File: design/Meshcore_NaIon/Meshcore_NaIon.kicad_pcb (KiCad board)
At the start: 2 copper layers, 90 x 100 mm, 136 parts, among them J10 AVR ISP 3V3, J11 LC OUT - SYS 3V3, J12 LTO 2S + MID -, J3 I2C3V3, J4 GPS / T114 P3, J5 UART3V3, J7 SOLAR 12V, J8 Na-ion 1S, M1 NiceNano_CLONE_MODIFIED, M2 HT-RA62, Q1 AO3401A, Q2 AO3401A, Q3 2N7002K, SW1 USER, SW2 RESET, U1 CN3722, U2 TPS63802DLAR, U4 DS3231MZ+TRL, U6 ATtiny13A-SSU, U7 SN74LVC2G125, U8 LMV431A, U9 LMV431A

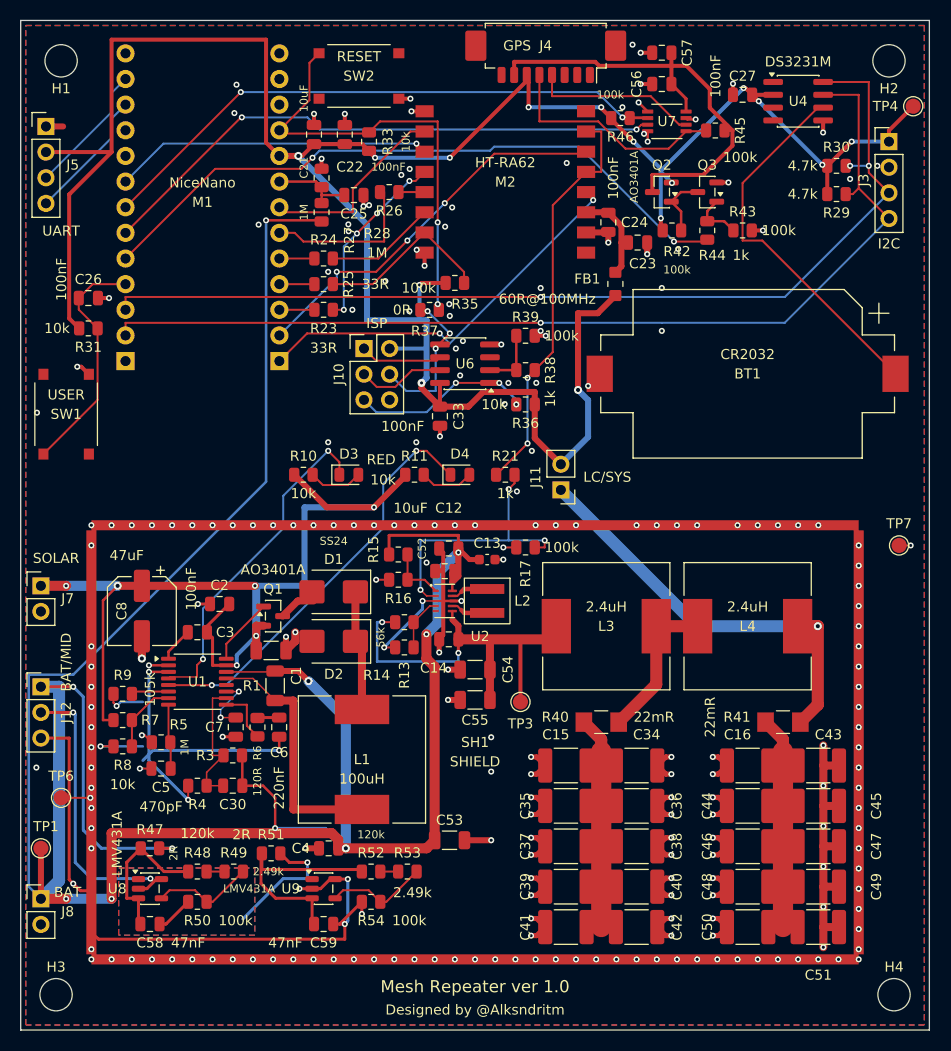
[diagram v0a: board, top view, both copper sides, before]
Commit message: Publish Mesh Repeater S4.16: routing fixes, COLD option and readable board labels
Update the editable KiCad project, seven-page schematic, portable footprints and 3D models, assembly variants, BOM, previews and independent CAD proofs. Preserve FakeTec GPIO compatibility. Manufacturing release remains paused.
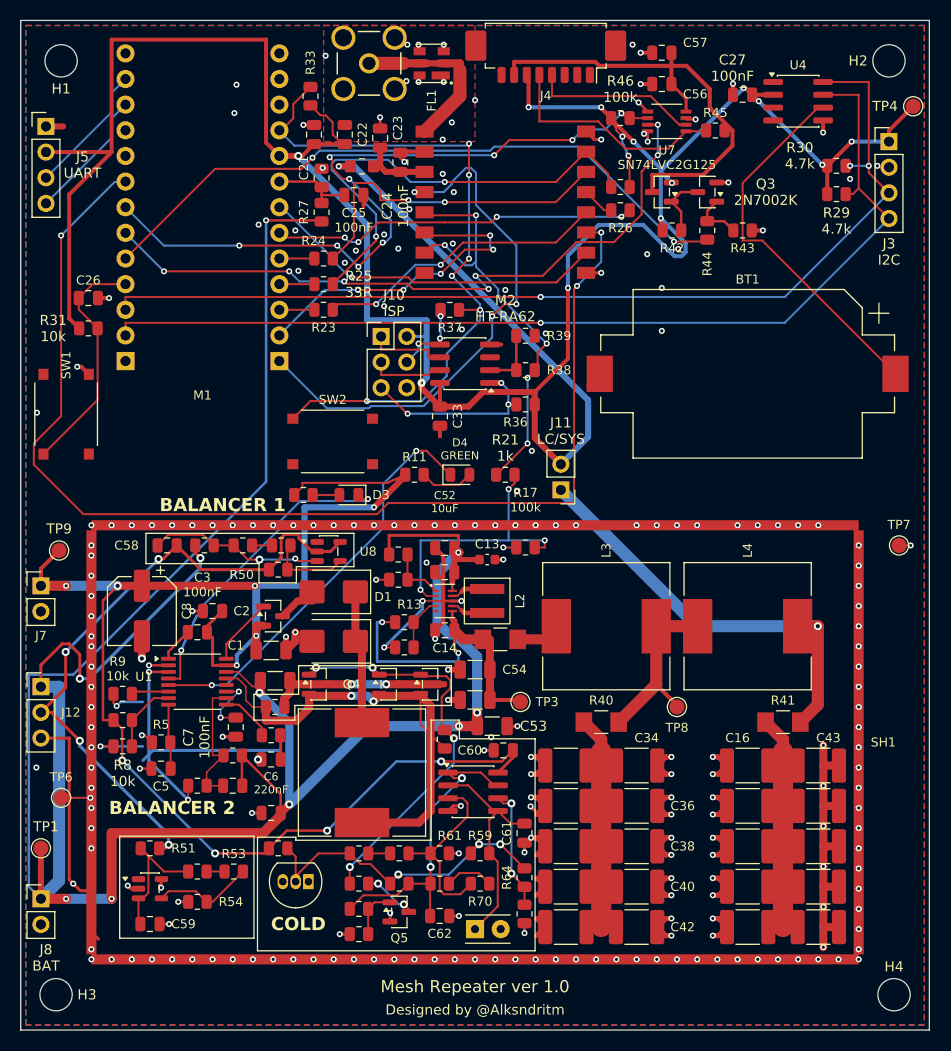
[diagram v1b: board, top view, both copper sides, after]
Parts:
- added C60: 100nF 100V X7R, Meshcore:C_0805_2012Metric, F.Cu at (47.8, 72.3)
- added C61: 1nF 100V C0G, Meshcore:C_0805_2012Metric, F.Cu at (49.9, 80.5)
- added C62: 100nF 100V X7R, Meshcore:C_0805_2012Metric, F.Cu at (41.5, 88.7)
- added FL1: S869M000S003, Meshcore:SAW_AEL_DCC6C_S869M000S003, F.Cu at (40.7, 4.25)
- added J13: SMA 50Ohm, Meshcore:SMA_KLS1_SMA002_B_Horizontal, F.Cu at (34.5, 4.25)
- added NT1: Cu link / cut for FL1, Meshcore:RF_Cut_Link_0p6, F.Cu at (40.7, 4.25)
- added Q4: AO3401A, Meshcore:SOT-23, F.Cu at (29.5, 65.8)
- added Q5: BSS138, Meshcore:SOT-23, F.Cu at (37.5, 88.3)
- added Q6: AO3401A, Meshcore:SOT-23, F.Cu at (36.5, 65.8)
- added Q7: AO3401A, Meshcore:SOT-23, F.Cu at (40.5, 65.8)
- added R55: 47mR 1%, Meshcore:R_Vishay_WSL1206_18, F.Cu at (47.5, 61.3)
- added R56: 1.8 ohm 1% 0.125W, Meshcore:R_0805_2012Metric, F.Cu at (25.2, 68.0)
- added R57: 47k 1% 0.125W, Meshcore:R_0805_2012Metric, F.Cu at (25.5, 82.0)
- added R58: 100k 1%, Meshcore:R_0805_2012Metric, F.Cu at (42.0, 71.2)
- added R59: 100k 1%, Meshcore:R_0805_2012Metric, F.Cu at (45.5, 82.5)
- added R60: 100k 1%, Meshcore:R_0805_2012Metric, F.Cu at (33.5, 82.5)
- added R61: 100k 1%, Meshcore:R_0805_2012Metric, F.Cu at (41.5, 82.5)
- added R62: 1M 1%, Meshcore:R_0805_2012Metric, F.Cu at (41.5, 85.5)
- added R63: 100k 1%, Meshcore:R_0805_2012Metric, F.Cu at (37.5, 85.5)
- added R64: 1.2M 1%, Meshcore:R_0805_2012Metric, F.Cu at (49.9, 84.9)
- added R65: 10k 1%, Meshcore:R_0805_2012Metric, F.Cu at (49.9, 88.5)
- added R66: 1k 1%, Meshcore:R_0805_2012Metric, F.Cu at (33.5, 88.0)
- added R67: 1M 1%, Meshcore:R_0805_2012Metric, F.Cu at (33.5, 90.5)
- added R68: 1k 1%, Meshcore:R_0805_2012Metric, F.Cu at (33.5, 85.5)
- added R69: 30k 1%, Meshcore:R_0805_2012Metric, F.Cu at (37.5, 82.5)
- added R70: 150k 1%, Meshcore:R_0805_2012Metric, F.Cu at (45.5, 85.5)
- added TH1: 10k NTC 1% B3988, Meshcore:NTC_TDK_B57861S_Onboard_or_Remote_P2.54mm, F.Cu at (45.0, 90.0)
- added TP8: FILTER_MID, Meshcore:TestPoint_Pad_D1.5mm, F.Cu at (65.0, 68.0)
- added TP9: SOLAR, Meshcore:TestPoint_Pad_D1.5mm, F.Cu at (3.80, 52.5)
- added U10: LM393XK, Meshcore:SOIC-8_3.9x4.9mm_P1.27mm, F.Cu at (44.8, 76.4)
- added U11: LM285Z-2.5G, Meshcore:TO-92_Inline, F.Cu at (28.5, 85.3)
- R27, R28: value 1M 0.1% -> 2.2M 0.1%
- R3: value 6.34k 0.1% -> 61.9k 0.1% <=25ppm/C
- R4: value 10k 0.1% -> 100k 0.1% <=25ppm/C
- moved U8 37.8 mm to (30.5, 52.6)
- moved C58 37.5 mm to (14.5, 52.0)
- moved SW2 36.3 mm to (30.9, 41.7)
- moved R50 33.9 mm to (25.5, 54.4)
- moved R49 32.6 mm to (25.8, 52.0)
- moved R48 32.6 mm to (22.0, 52.0)
- moved R47 30.5 mm to (18.2, 52.0), turned to 0 degrees
- moved FB1 27.7 mm to (33.8, 14.4), turned to 0 degrees
- moved C23 27.5 mm to (35.6, 11.7), turned to 90 degrees
- moved R26 23.0 mm to (59.4, 18.8), turned to 0 degrees
- moved C24 21.4 mm to (37.6, 14.1), turned to 90 degrees
- moved R35 19.0 mm to (59.4, 16.5), turned to 180 degrees
- moved R52 17.2 mm to (17.5, 84.3)
- moved R54 17.2 mm to (17.5, 87.3)
- moved C59 17.2 mm to (12.8, 89.5)
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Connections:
- L1 pad 2: /CS_P -> CS_P
- L3 pad 1: /2. Converter/SYS_PRE -> /2. Converter/SYS_LC_IN
- M2 pad 1: unconnected-(M2-ANT_/_IPEX_used-Pad1) -> /3. Modules/ANT_RF
- R1 pad 1: /CS_P -> CHG_CS_M
- U1 pad 13: /CS_P -> CS_P
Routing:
- net /3. Modules/RADIO_RXEN: track 31.5 -> 117.9 mm, vias 1 -> 3
- net SOLAR: track 91.0 -> 151.0 mm, vias 6 -> 10
- net CS_P: track 0.00 -> 50.8 mm, vias 0 -> 2
- net CHG_G_SHUNT: track 0.00 -> 40.2 mm, vias 0 -> 4
- net SYS_3V3: track 246.5 -> 285.0 mm
- net GND: track 269.8 -> 231.3 mm, vias 239 -> 240
- net /7. Thermal/CHG_VREF: track 0.00 -> 32.9 mm, vias 0 -> 3
- net /7. Thermal/CHG_WARM: track 0.00 -> 31.1 mm, vias 0 -> 2
- net Net-(M2-NSS): track 17.8 -> 47.6 mm, vias 0 -> 2
- net MCU_RESET: track 44.3 -> 70.8 mm, vias 2 -> 6
- net /CS_P: track 25.1 -> 0.00 mm
- net Net-(M2-MOSI): track 11.0 -> 34.0 mm, vias 0 -> 2
- net /7. Thermal/CHG_TSENSE: track 0.00 -> 22.5 mm
- net Net-(M1-P0.02_/_MISO): track 15.6 -> 36.4 mm, vias 0 -> 4
- net BAT: track 282.7 -> 262.4 mm
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- removed copper zone on B.Cu, net LTO_MID
- removed copper zone on F.Cu, net LTO_MID
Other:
- board text added: "1 NTC"
- board text added: "1 RF"
- board text added: "BAL1 x1.5"
- board text added: "BAL2 x1.25"
- board text added: "BALANCER 1"
- board text added: "BALANCER 2"
- board text added: "BT1"
- board text added: "BT1 CR2032"
- board text added: "C1"
- board text added: "C1 10uF"
- board text added: "C12 10uF"
- board text added: "C13"
- board text added: "C13 100nF"
- board text added: "C14"
- board text added: "C14 22uF"
- board text added: "C15 100uF"
- board text added: "C16"
- board text added: "C16 100uF"
- board text added: "C2"
- board text added: "C2 100nF"
- board text added: "C21"
- board text added: "C21 10uF"
- board text added: "C22"
- board text added: "C22 100nF"
- board text added: "C23"
- board text added: "C23 22uF"
- board text added: "C24 100nF"
- board text added: "C25 100nF"
- board text added: "C26"
- board text added: "C26 100nF"
- board text added: "C27 100nF"
- board text added: "C3 100nF"
- board text added: "C30 Na:12pF LTO:6.8pF"
- board text added: "C33"
- board text added: "C33 100nF"
- board text added: "C34"
- board text added: "C34 100uF"
- board text added: "C35 100uF"
- board text added: "C36"
- board text added: "C36 100uF"
- board text added: "C37 100uF"
- board text added: "C38"
- board text added: "C38 100uF"
- board text added: "C39 100uF"
- board text added: "C40"
- board text added: "C40 100uF"
- board text added: "C41 100uF"
- board text added: "C42"
- board text added: "C42 100uF"
- board text added: "C43"
- board text added: "C43 100uF"
- board text added: "C44 100uF"
- board text added: "C45 100uF"
- board text added: "C46 100uF"
- board text added: "C47 100uF"
- board text added: "C48 100uF"
- board text added: "C49 100uF"
- board text added: "C5"
- board text added: "C5 470pF"
- board text added: "C50 100uF"
- board text added: "C51 100uF"
- board text added: "C52 10uF"
- board text added: "C53"
- board text added: "C54"
- board text added: "C55"
- board text added: "C56"
- board text added: "C56 100nF"
- board text added: "C57"
- board text added: "C57 10uF"
- board text added: "C58"
- board text added: "C58 47nF"
- board text added: "C59"
- board text added: "C59 47nF"
- board text added: "C6 220nF"
- board text added: "C60"
- board text added: "C60 100nF"
- board text added: "C61"
- board text added: "C61 1nF"
- board text added: "C62"
- board text added: "C62 100nF"
- board text added: "C7 100nF"
- board text added: "C8"
- board text added: "C8 47uF"
- board text added: "CHG x1.25"
- board text added: "CHG x1.5"
- board text added: "CHG x1.75"
- board text added: "COLD"
- board text added: "COLD x1.25"
- board text added: "COLD x1.5"
- board text added: "COLD x1.75"
- board text added: "D1"
- board text added: "D1 SS24"
- board text added: "D2 SS24"
- board text added: "D3"
- board text added: "D3 RED"
- board text added: "D4 GREEN"
- board text added: "FB1 60R@100MHz"
- board text added: "FL1"
- board text added: "FL1 S869M000S003"
- board text added: "H1"
- board text added: "H2"
- board text added: "H3"
- board text added: "H4"
- board text added: "J12"
- board text added: "J12 BAT/ MID"
- board text added: "J13 SMA"
- board text added: "J4"
- board text added: "J7"
- board text added: "L1 100uH"
- board text added: "L2"
- board text added: "L2 0.47uH"
- board text added: "L3"
- board text added: "L3 2.4uH"
- board text added: "L4"
- board text added: "L4 2.4uH"
- board text added: "LC x1.25"
- board text added: "M1"
- board text added: "M1 NiceNano"
- board text added: "M2 HT-RA62"
- board text added: "NT1"
- board text added: "PARTS x1.25"
- board text added: "PARTS x1.5"
- board text added: "Q1 AO3401A"
- board text added: "Q2 AO3401A"
- board text added: "Q3 2N7002K"
- board text added: "Q4"
- board text added: "Q4 AO3401A"
- board text added: "Q5"
- board text added: "Q5 BSS138"
- board text added: "Q6 AO3401A"
- board text added: "Q7 AO3401A"
- board text added: "R1 0.28R"
- board text added: "R10 10k"
- board text added: "R11"
- board text added: "R11 10k"
- board text added: "R13"
- board text added: "R13 56k"
- board text added: "R14 10k"
- board text added: "R15 Na:40.2k LTO:130k"
- board text added: "R16 Na:49.9k LTO:49.9k"
- board text added: "R17 100k"
- board text added: "R21 1k"
- board text added: "R23"
- board text added: "R23 33R"
- board text added: "R24"
- board text added: "R24 33R"
- board text added: "R25 33R"
- board text added: "R26"
- board text added: "R26 33R"
- board text added: "R27"
- board text added: "R27 2.2M"
- board text added: "R28 2.2M"
- board text added: "R29 4.7k"
- board text added: "R3 Na:61.9k LTO:121k"
- board text added: "R30 4.7k"
- board text added: "R31 10k"
- board text added: "R33"
- board text added: "R33 10k"
- board text added: "R35 100k"
- board text added: "R36"
- board text added: "R36 10k"
- board text added: "R37"
- board text added: "R37 0R"
- board text added: "R38"
- board text added: "R38 1k"
- board text added: "R39"
- board text added: "R39 100k"
- board text added: "R4 Na:100k LTO:100k"
- board text added: "R40"
- board text added: "R40 22mR"
- board text added: "R41"
- board text added: "R41 22mR"
- board text added: "R42"
- board text added: "R42 100k"
- board text added: "R43"
- board text added: "R43 100k"
- board text added: "R44"
- board text added: "R44 1k"
- board text added: "R45"
- board text added: "R45 100k"
- board text added: "R46 100k"
- board text added: "R47 2R"
- board text added: "R48 120k"
- board text added: "R49 2.49k"
- board text added: "R5"
- board text added: "R5 1M"
- board text added: "R50"
- board text added: "R50 100k"
- board text added: "R51"
- board text added: "R51 2R"
- board text added: "R52 120k"
- board text added: "R53"
- board text added: "R53 2.49k"
- board text added: "R54"
- board text added: "R54 100k"
- board text added: "R55 47mR"
- board text added: "R56 Na:1.8R LTO:0R"
- board text added: "R57 47k"
- board text added: "R58 100k"
- board text added: "R59"
- board text added: "R59 100k"
- board text added: "R6 120R"
- board text added: "R60 100k"
- board text added: "R61"
- board text added: "R61 100k"
- board text added: "R62 1M"
- board text added: "R63 100k"
- board text added: "R64"
- board text added: "R64 1.2M"
- board text added: "R65 10k"
- board text added: "R66 1k"
- board text added: "R67 1M"
- board text added: "R68 1k"
- board text added: "R69 30k"
- board text added: "R7 105k"
- board text added: "R70"
- board text added: "R70 150k"
- board text added: "R8 10k"
- board text added: "R9 10k"
- board text added: "RF x1.25"
- board text added: "SH1"
- board text added: "SH1 SHIELD"
- board text added: "SW1"
- board text added: "SW1 USER"
- board text added: "SW2"
- board text added: "SW2 RESET"
- board text added: "TH1 10k NTC"
- board text added: "TH1 NTC"
- board text added: "TP1"
- board text added: "TP3"
- board text added: "TP4"
- board text added: "TP6"
- board text added: "TP7"
- board text added: "TP8"
- board text added: "TP9"
- board text added: "TPS x1.25"
- board text added: "TPS x1.5"
- board text added: "U1"
- board text added: "U1 CN3722"
- board text added: "U10 LM393XK"
- board text added: "U11 LM285Z-2.5G"
- board text added: "U2 TPS63802DLAR"
- board text added: "U4"
- board text added: "U4 DS3231M"
- board text added: "U7 SN74LVC2G125"
- board text added: "U8"
- board text added: "U8 LMV431A"
- board text added: "U9 LMV431A"
- board text added: "WDT x1.25"
- board text removed: "C1 10uF C3 100nF C7 100nF R1 0.28R R9 10k U1 CN3722"
- board text removed: "C13 100nF C14 22uF C52 10uF D2 SS24 D4 GREEN L2 0.47uH R14 10k U2 TPS63802DLAR"
- board text removed: "C15 100uF C34 100uF C35 100uF C36 100uF C37 100uF C38 100uF C39 100uF C40 100uF C41 100uF C42 100uF"
- board text removed: "C16 100uF C43 100uF C44 100uF C45 100uF C46 100uF C47 100uF C48 100uF C49 100uF C50 100uF C51 100uF"
- board text removed: "C23 22uF C56 100nF C57 10uF Q3 2N7002K U7 SN74LVC2G125"
- board text removed: "C25 100nF R24 33R R26 33R"
- board text removed: "C30 Na:12pF LTO:6.8pF R3 Na:6.34k LTO:13k R4 Na:10k LTO:10.5k"
- board text removed: "R15 Na:40.2k LTO:130k R16 Na:49.9k LTO:49.9k"

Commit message: Publish S4.21 PCB and validated Rezonit manufacturing package
Update the public project to the accepted single-board S4.21 design, keeping
the user's manual routing improvements and removing SH1 and TP6.

Include the full editable KiCad project and local assets, three assembly BOM
variants, current assembly notes, eight-page schematic PDF, board views and
a clean nine-file Gerber/Excellon ZIP for Rezonit.

Validation: layout 29/29, power 14/14, CAM 59/59, publication integrity 18/18.
The committed native board and manufacturing ZIP match the verified byte
hashes. Preserve the existing licensing notices and watchdog source.
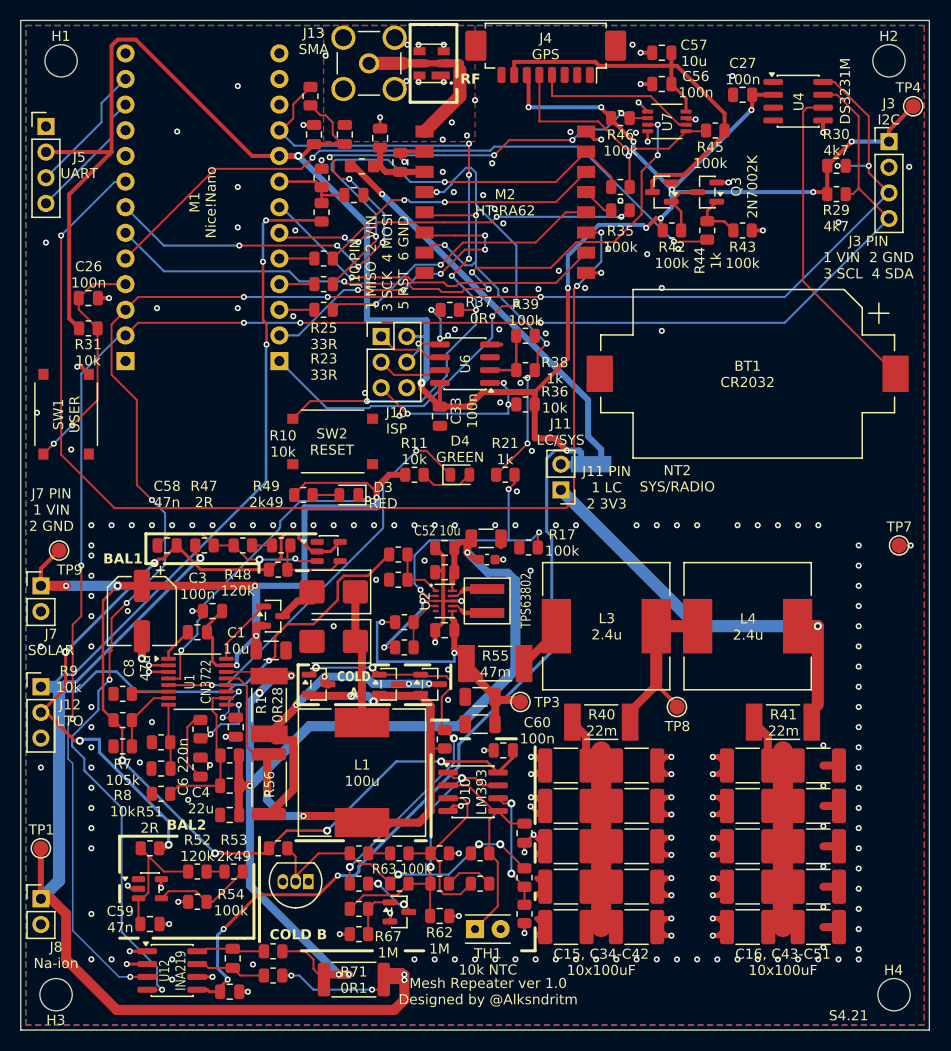
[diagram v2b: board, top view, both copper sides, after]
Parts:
- removed SH1: CUSTOM_SHIELD_FRAME, Meshcore:Shield_Frame_76x43
- removed TP6: GND, Meshcore:TestPoint_Pad_D1.5mm
- added C63: 100nF 50V X7R, Meshcore:C_0805_2012Metric, F.Cu at (20.7, 96.2)
- added C64: 100nF 50V X7R, Meshcore:C_0805_2012Metric, F.Cu at (21.0, 92.9)
- added NT2: 3V3 STAR, Meshcore:NetTie_2_SMD_Power_Star_A3, B.Cu at (56.5, 44.0)
- added R71: 0.1R 1% 1W, Meshcore:R_2512_6332Metric__A3_R71, F.Cu at (33.0, 95.0)
- added R72: 10R 1%, Meshcore:R_0805_2012Metric, F.Cu at (25.0, 92.2)
- added R73: 10R 1%, Meshcore:R_0805_2012Metric, F.Cu at (25.0, 94.6)
- added U12: INA219AIDR, Meshcore:SOIC-8_3.9x4.9mm_P1.27mm, F.Cu at (15.0, 94.1)
- R1: footprint Meshcore:R_1206_3216Metric -> Meshcore:R_Vishay_WSL2512_A3__A3_R1
- R40: footprint Meshcore:R_Vishay_WSL1206_18 -> Meshcore:R_Vishay_WSL2512_A3__A3_R40
- R41: footprint Meshcore:R_Vishay_WSL1206_18 -> Meshcore:R_Vishay_WSL2512_A3__A3_R41
- R55: footprint Meshcore:R_Vishay_WSL1206_18 -> Meshcore:R_Vishay_WSL2512_A3__A3_R55
- R56: value 1.8 ohm 1% 0.125W -> 1.8R 1% 1W; footprint Meshcore:R_0805_2012Metric -> Meshcore:R_2512_6332Metric__A3_R56
- moved C53 18.6 mm to (46.1, 51.3)
- moved R56 7.67 mm to (24.6, 75.7), turned to -90 degrees
- moved C6 7.04 mm to (17.8, 74.0), turned to 90 degrees
- moved R6 7.03 mm to (17.8, 70.2), turned to 90 degrees
- moved C4 4.10 mm to (20.7, 78.7)
- moved R4 3.69 mm to (13.9, 76.6)
- moved C54 2.75 mm to (45.5, 67.0)
- moved R1 2.47 mm to (24.6, 67.8), turned to 90 degrees
- moved C55 2.45 mm to (45.5, 69.7)
- moved R55 2.45 mm to (47.0, 63.7)
- moved C30 0.30 mm to (20.7, 75.8)
- moved R3 0.30 mm to (20.7, 72.8)
- moved R17 0.30 mm to (50.3, 52.2)
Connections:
- net /3. Modules/RADIO_3V3 renamed /3. Modules/RADIO_LOCAL_3V3
- C12 pad 1: BAT -> BAT_SYS
- C13 pad 1: BAT -> BAT_SYS
- C30 pad 1: BAT -> BAT_SYS
- C4 pad 1: BAT -> BAT_SYS
- C52 pad 1: BAT -> BAT_SYS
- C53 pad 1: BAT -> BAT_SYS
- FB1 pad 1: SYS_3V3 -> RADIO_3V3
- R1 pad 2: BAT -> BAT_SYS
- R3 pad 1: BAT -> BAT_SYS
- U1 pad 14: BAT -> BAT_SYS
- U2 pad 10: BAT -> BAT_SYS
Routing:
- net BAT_SYS: track 0.00 -> 114.4 mm, vias 0 -> 6
- net GND: track 231.3 -> 135.4 mm, vias 240 -> 237
- net SCL: track 99.8 -> 177.7 mm, vias 3 -> 9
- net SDA: track 99.7 -> 168.8 mm, vias 1 -> 6
- net BAT: track 262.4 -> 214.2 mm, vias 10 -> 9
- net RADIO_3V3: track 0.00 -> 40.0 mm, vias 0 -> 1
- net SYS_3V3: track 285.0 -> 312.4 mm, vias 15 -> 17
- net CHG_CS_M: track 17.8 -> 32.7 mm, vias 2 -> 4
- net Net-(U12-IN-): track 0.00 -> 7.08 mm
- net Net-(U12-IN+): track 0.00 -> 6.82 mm
- net CS_P: track 50.8 -> 56.9 mm, vias 2 -> 4
- net /4. RTC_IO/RTC_BAT: track 37.4 -> 31.9 mm
- net Net-(M2-MOSI): track 34.0 -> 28.9 mm
- net /3. Modules/RADIO_RXEN: track 117.9 -> 112.8 mm
- net Net-(C6-Pad1): track 2.42 -> 7.35 mm
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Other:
- board text added: "BAL1"
- board text added: "BAL2"
- board text added: "C1 10u"
- board text added: "C12 10u"
- board text added: "C13 100n"
- board text added: "C14 22u"
- board text added: "C15, C34-C42 10x100uF"
- board text added: "C16, C43-C51 10x100uF"
- board text added: "C2 100n"
- board text added: "C21 10u"
- board text added: "C22 100n"
- board text added: "C23 22u"
- board text added: "C24 100n"
- board text added: "C25 100n"
- board text added: "C26 100n"
- board text added: "C27 100n"
- board text added: "C3 100n"
- board text added: "C30 N12p L6.8p"
- board text added: "C33 100n"
- board text added: "C4 22u"
- board text added: "C5 470p"
- board text added: "C52 10u"
- board text added: "C53 DNP"
- board text added: "C54 DNP"
- board text added: "C55 DNP"
- board text added: "C56 100n"
- board text added: "C57 10u"
- board text added: "C58 47n"
- board text added: "C59 47n"
- board text added: "C6 220n"
- board text added: "C60 100n"
- board text added: "C61 1n"
- board text added: "C62 100n"
- board text added: "C63 100n"
- board text added: "C64 100n"
- board text added: "C7 100n"
- board text added: "C8 47u"
- board text added: "COLD A"
- board text added: "COLD B"
- board text added: "DS3231M"
- board text added: "FB1 60R"
- board text added: "FL1 S869M000 S003 NT1 CUT"
- board text added: "J10 PIN 1 MISO 2 VIN 3 SCK 4 MOSI 5 RST 6 GND"
- board text added: "J11 PIN 1 LC 2 3V3"
- board text added: "J12 PIN 1 BAT+ 2 MID 3 GND"
- board text added: "J13 PIN 1 RF 2 GND"
- board text added: "J3 PIN 1 VIN 2 GND 3 SCL 4 SDA"
- board text added: "J4 PIN 1 NC 2 NC 3 NC 4 RX 5 TX 6 BACKUP 7 POWER 8 GND"
- board text added: "J5 PIN UART 1 GND 2 VIN 3 TX 4 RX"
- board text added: "J7 PIN 1 VIN 2 GND"
- board text added: "J8 Na-ion"
- board text added: "J8 PIN 1 BAT+ 2 GND"
- board text added: "L1 100u"
- board text added: "L2 0.47u"
- board text added: "L3 2.4u"
- board text added: "L4 2.4u"
- board text added: "M1 Nice!Nano"
- board text added: "Mesh Repeater ver 1.0 Designed by @Alksndritm"
- board text added: "N: Na-ion / L: LTO 2S"
- board text added: "NT2 SYS/RADIO"
- board text added: "R1 0R28"
- board text added: "R15 N40k2 L130k"
- board text added: "R16 49k9"
- board text added: "R27 2M2"
- board text added: "R28 2M2"
- board text added: "R29 4k7"
- board text added: "R3 N61k9 L121k"
- board text added: "R30 4k7"
- board text added: "R4 100k"
- board text added: "R40 22m"
- board text added: "R41 22m"
- board text added: "R49 2k49"
- board text added: "R53 2k49"
- board text added: "R55 47m"
- board text added: "R56"
- board text added: "R56 N1R8 L0R"
- board text added: "R56: 0R без ХОЛОДА"
- board text added: "R64 1M2"
- board text added: "R71 0R1"
- board text added: "R72 10R"
- board text added: "R73 10R"
- board text added: "RF"
- board text added: "S4.21"
- board text added: "TPS63802"
- board text added: "U10 LM393"
- board text added: "U11 LM285-2.5"
- board text added: "U12 INA219"
- board text added: "U2"
- board text added: "U6"
- board text added: "U7"
- board text added: "U7 74LVC2G125"
- board text added: "U8 LMV 431A"
- board text added: "USB: снять J11"
- board text removed: "1"
- board text removed: "1 BAT+"
- board text removed: "1 GND"
- board text removed: "1 LC_OUT"
- board text removed: "1 MISO"
- board text removed: "1 NC/RST"
- board text removed: "1 NTC"
- board text removed: "1 RF"
- board text removed: "1 SOLAR+"
- board text removed: "1 VIN"
- board text removed: "2"
- board text removed: "2 GND"
- board text removed: "2 MID"
- board text removed: "2 NC/PPS"
- board text removed: "2 SYS_3V3"
- board text removed: "2 VIN"
- board text removed: "3"
- board text removed: "3 GND"
- board text removed: "3 NC/WAKE"
- board text removed: "3 SCK"
- board text removed: "3 SCL"
- board text removed: "3 TX"
- board text removed: "4"
- board text removed: "4 MOSI"
- board text removed: "4 RX"
- board text removed: "4 SDA"
- board text removed: "5"
- board text removed: "5 RESET"
- board text removed: "5 TX"
- board text removed: "6"
- board text removed: "6 BACKUP"
- board text removed: "6 GND"
- board text removed: "7"
- board text removed: "7 POWER"
- board text removed: "8"
- board text removed: "8 GND"
- board text removed: "BAL1 x1.5"
- board text removed: "BAL2 x1.25"
- board text removed: "BALANCER 1"
- board text removed: "BALANCER 2"
- board text removed: "BT1"
- board text removed: "BT1 +"
- board text removed: "BT1 -"
- board text removed: "C1"
- board text removed: "C1 10uF"
- board text removed: "C12 10uF"
- board text removed: "C13"
- board text removed: "C13 100nF"
- board text removed: "C14"
- board text removed: "C14 22uF"
- board text removed: "C15 100uF"
- board text removed: "C16"
- board text removed: "C16 100uF"
- board text removed: "C2"
- board text removed: "C2 100nF"
- board text removed: "C21"
- board text removed: "C21 10uF"
- board text removed: "C22"
- board text removed: "C22 100nF"
- board text removed: "C23"
- board text removed: "C23 22uF"
- board text removed: "C24 100nF"
- board text removed: "C25 100nF"
- board text removed: "C26"
- board text removed: "C26 100nF"
- board text removed: "C27 100nF"
- board text removed: "C3 100nF"
- board text removed: "C30 Na:12pF LTO:6.8pF"
- board text removed: "C33"
- board text removed: "C33 100nF"
- board text removed: "C34"
- board text removed: "C34 100uF"
- board text removed: "C35 100uF"
- board text removed: "C36"
- board text removed: "C36 100uF"
- board text removed: "C37 100uF"
- board text removed: "C38"
- board text removed: "C38 100uF"
- board text removed: "C39 100uF"
- board text removed: "C4 22uF"
- board text removed: "C40"
- board text removed: "C40 100uF"
- board text removed: "C41 100uF"
- board text removed: "C42"
- board text removed: "C42 100uF"
- board text removed: "C43"
- board text removed: "C43 100uF"
- board text removed: "C44 100uF"
- board text removed: "C45 100uF"
- board text removed: "C46 100uF"
- board text removed: "C47 100uF"
- board text removed: "C48 100uF"
- board text removed: "C49 100uF"
- board text removed: "C5"
- board text removed: "C5 470pF"
- board text removed: "C50 100uF"
- board text removed: "C51 100uF"
- board text removed: "C52 10uF"
- board text removed: "C53"
- board text removed: "C54"
- board text removed: "C55"
- board text removed: "C56"
- board text removed: "C56 100nF"
- board text removed: "C57"
- board text removed: "C57 10uF"
- board text removed: "C58"
- board text removed: "C58 47nF"
- board text removed: "C59"
- board text removed: "C59 47nF"
- board text removed: "C6 220nF"
- board text removed: "C60"
- board text removed: "C60 100nF"
- board text removed: "C61"
- board text removed: "C61 1nF"
- board text removed: "C62"
- board text removed: "C62 100nF"
- board text removed: "C7 100nF"
- board text removed: "C8"
- board text removed: "C8 47uF"
- board text removed: "CHG x1.25"
- board text removed: "CHG x1.5"
- board text removed: "CHG x1.75"
- board text removed: "COLD"
- board text removed: "COLD x1.25"
- board text removed: "COLD x1.5"
- board text removed: "COLD x1.75"
- board text removed: "CUSTOM LID 76x43 H14"
- board text removed: "D1"
- board text removed: "D3"
- board text removed: "Designed by @Alksndritm"
- board text removed: "FB1 60R@100MHz"
- board text removed: "FL1"
- board text removed: "FL1 S869M000S003"
- board text removed: "J12"
- board text removed: "J12 BAT/ MID"
- board text removed: "J4"
- board text removed: "J7"
- board text removed: "J8 BAT"
- board text removed: "L1 100uH"
- board text removed: "L2"
- board text removed: "L2 0.47uH"
- board text removed: "L3"
- board text removed: "L3 2.4uH"
- board text removed: "L4"
- board text removed: "L4 2.4uH"
- board text removed: "LC x1.25"
- board text removed: "M1"
- board text removed: "M1 NiceNano"
- board text removed: "Mesh Repeater ver 1.0"
- board text removed: "NT1"
- board text removed: "PARTS x1.25"
- board text removed: "PARTS x1.5"
- board text removed: "Q4"
- board text removed: "Q5"
- board text removed: "R1 0.28R"
- board text removed: "R11"
- board text removed: "R13"
- board text removed: "R15 Na:40.2k LTO:130k"
- board text removed: "R16 Na:49.9k LTO:49.9k"
- board text removed: "R23"
- board text removed: "R24"
- board text removed: "R26"
- board text removed: "R27"
- board text removed: "R27 2.2M"
- board text removed: "R28 2.2M"
- board text removed: "R29 4.7k"
- board text removed: "R3 Na:61.9k LTO:121k"
- board text removed: "R30 4.7k"
- board text removed: "R33"
- board text removed: "R36"
- board text removed: "R37"
- board text removed: "R38"
- board text removed: "R39"
- board text removed: "R4 Na:100k LTO:100k"
- board text removed: "R40"
- board text removed: "R40 22mR"
- board text removed: "R41"
- board text removed: "R41 22mR"
- board text removed: "R42"
- board text removed: "R43"
- board text removed: "R44"
- board text removed: "R45"
- board text removed: "R49 2.49k"
- board text removed: "R5"
- board text removed: "R50"
- board text removed: "R51"
- board text removed: "R53"
- board text removed: "R53 2.49k"
- board text removed: "R54"
- board text removed: "R55 47mR"
- board text removed: "R56 Na:1.8R LTO:0R"
- board text removed: "R59"
- board text removed: "R61"
- board text removed: "R64"
- board text removed: "R64 1.2M"
- board text removed: "R70"
- board text removed: "RF x1.25"
- board text removed: "SH1"
- board text removed: "SH1 SHIELD"
- board text removed: "SW1"
- board text removed: "SW2"
- board text removed: "TH1 NTC"
- board text removed: "TP6"
- board text removed: "TPS x1.25"
- board text removed: "TPS x1.5"
- board text removed: "U1"
- board text removed: "U10 LM393XK"
- board text removed: "U11 LM285Z-2.5G"
- board text removed: "U2 TPS63802DLAR"
- board text removed: "U4 DS3231M"
- board text removed: "U7 SN74LVC2G125"
- board text removed: "U8"
- board text removed: "U8 LMV431A"
- board text removed: "WDT x1.25"
